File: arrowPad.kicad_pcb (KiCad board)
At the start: 2 copper layers, 59 x 61 mm, 22 parts, among them K1 KEYSW, K2 KEYSW, K3 KEYSW, K4 KEYSW, K5 KEYSW, K6 KEYSW, K7 KEYSW, K8 KEYSW, K9 KEYSW, SW1 SW_DIP_x01, U1 ProMicro, U2 NRF24L01_Breakout

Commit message: added cu ground plane
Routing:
- net /GND1: track 36.0 -> 1.33 mm
- added copper zone on F.Cu, net /GND1
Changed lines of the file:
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@@
     (thickness 1.6)
     (drawings 4)
-    (tracks 233)
+    (tracks 224)
     (zones 0)
     (modules 22)
@@
   (segment (start 80.78 83.63) (end 62.77 83.63) (width 0.25) (layer B.Cu) (net 1))
   (segment (start 61.25 104.52) (end 61.498462 104.52) (width 0.25) (layer F.Cu) (net 2))
-  (segment (start 60.542894 104.52) (end 59.1 103.077106) (width 0.25) (layer B.Cu) (net 2))
   (segment (start 61.25 104.52) (end 60.542894 104.52) (width 0.25) (layer B.Cu) (net 2))
   (via (at 59.1 102.7) (size 0.8) (drill 0.4) (layers F.Cu B.Cu) (net 2))
   (segment (start 59.1 103.077106) (end 59.1 102.7) (width 0.25) (layer B.Cu) (net 2))
-  (segment (start 59.1 95.64) (end 61.8 92.94) (width 0.25) (layer F.Cu) (net 2))
-  (segment (start 59.1 102.7) (end 59.1 95.64) (width 0.25) (layer F.Cu) (net 2))
-  (segment (start 61.8 92.94) (end 62.84 91.9) (width 0.25) (layer F.Cu) (net 2))
-  (segment (start 62.84 91.9) (end 63.3 91.9) (width 0.25) (layer F.Cu) (net 2))
-  (segment (start 63.3 91.9) (end 66.7 88.5) (width 0.25) (layer F.Cu) (net 2))
-  (segment (start 66.7 88.5) (end 72.2 88.5) (width 0.25) (layer F.Cu) (net 2))
-  (segment (start 74.53 86.17) (end 80.78 86.17) (width 0.25) (layer F.Cu) (net 2))
-  (segment (start 72.2 88.5) (end 74.53 86.17) (width 0.25) (layer F.Cu) (net 2))
   (segment (start 43.725 97.375) (end 43.725 96.25) (width 0.25) (layer B.Cu) (net 3))
   (segment (start 48.1 101.75) (end 43.725 97.375) (width 0.25) (layer B.Cu) (net 3))
@@
   (segment (start 61.8 87.55) (end 61.8 90.4) (width 0.25) (layer B.Cu) (net 30))
   (segment (start 59.86 85.61) (end 61.8 87.55) (width 0.25) (layer B.Cu) (net 30))
+  (zone (net 2) (net_name /GND1) (layer F.Cu) (hatch edge 0.508)
+    (connect_pads (clearance 0.254))
+    (min_thickness 0.254)
+    (fill yes (arc_segments 16) (thermal_gap 0.508) (thermal_bridge_width 0.508))
+    (polygon
+      (pts
+        (xy 100.2 81.4) (xy 100.2 142.7) (xy 40.8 142.7) (xy 40.8 81.3)
+      )
+    )
+  )
 )

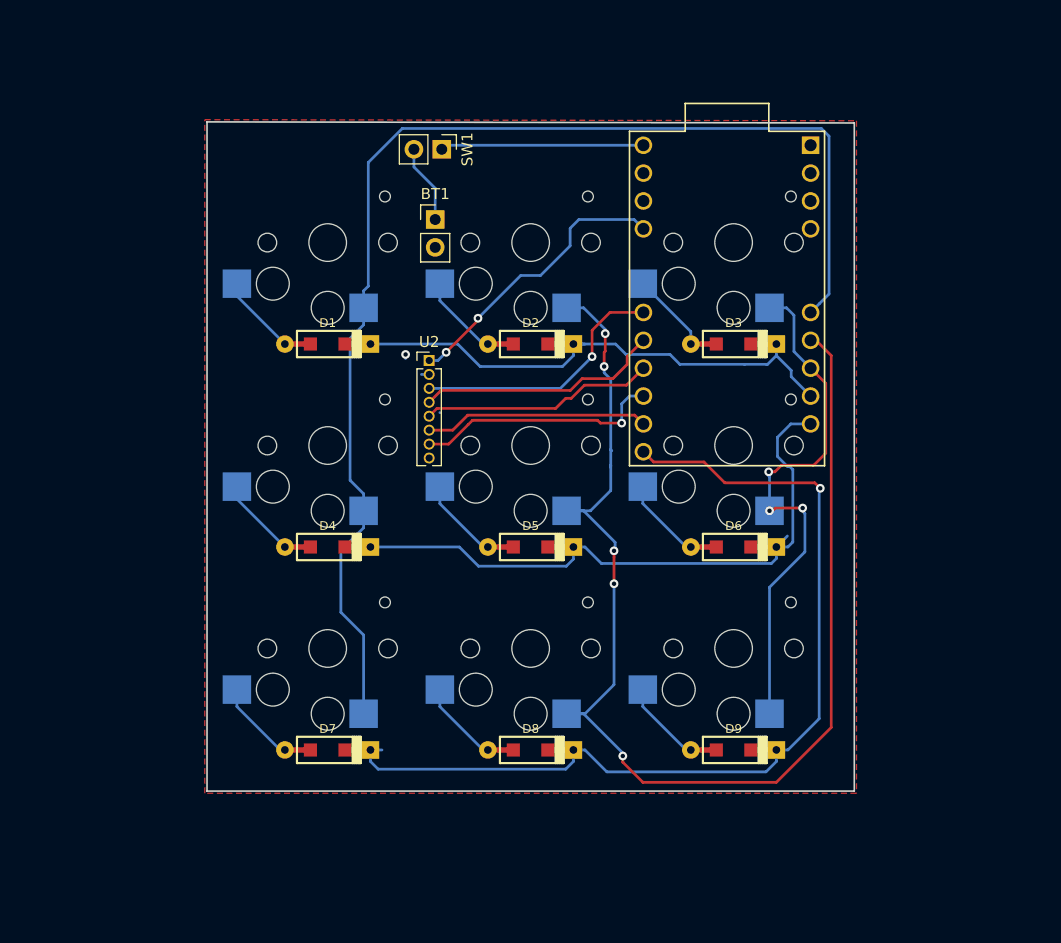
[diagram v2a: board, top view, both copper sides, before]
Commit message: added status led
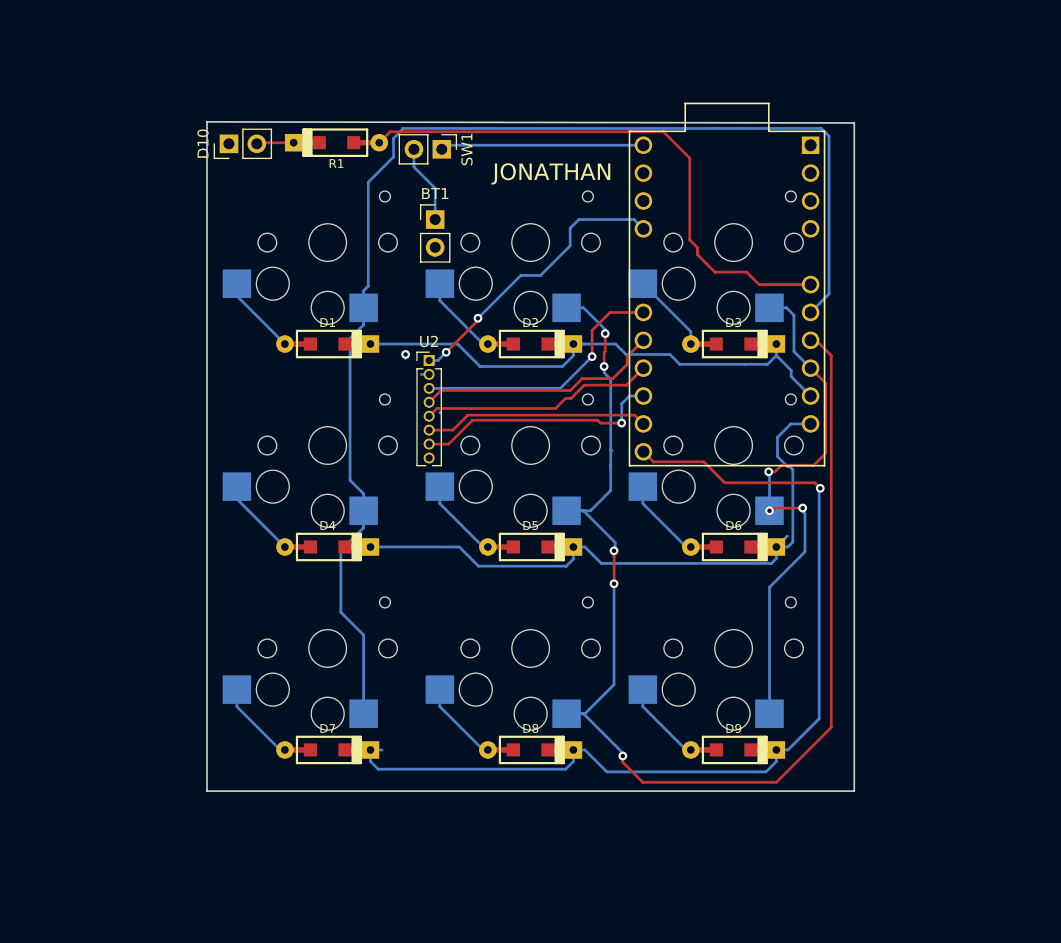
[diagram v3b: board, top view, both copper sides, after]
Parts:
- added D10: LED, Connector_PinHeader_2.54mm:PinHeader_1x02_P2.54mm_Vertical, F.Cu at (43.0, 83.5)
- added R1: R, keyboard_parts:D_SOD123_axial, F.Cu at (52.8, 83.4)
- U1: footprint promicro:proMicrov3 -> Transformer_SMD:proMicrov6
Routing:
- net Net-(R1-Pad2): track 0.00 -> 50.2 mm
- net Net-(D10-Pad2): track 0.00 -> 3.40 mm
- removed copper zone on F.Cu, net /GND1
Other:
- board text added: "JONATHAN"

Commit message: added drill holes
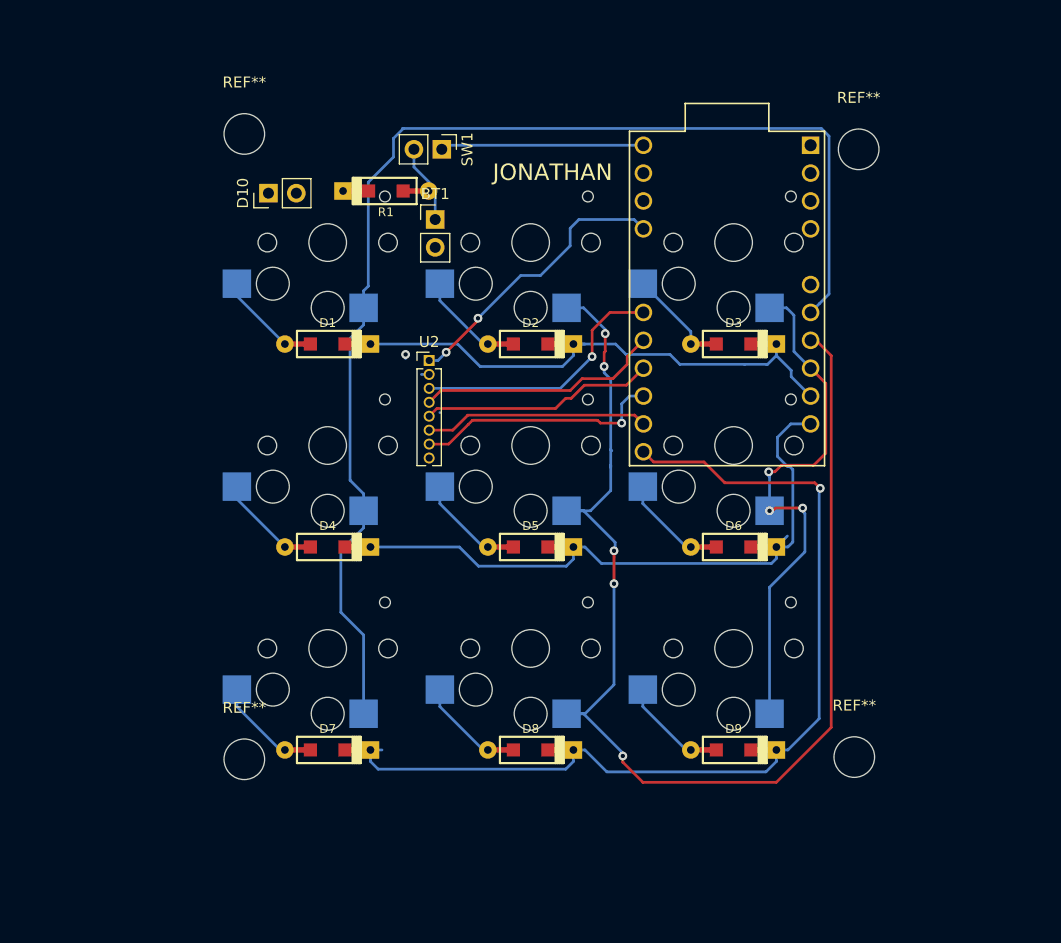
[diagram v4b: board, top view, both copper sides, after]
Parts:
- added REF**: MountingHole_3.7mm, MountingHole:MountingHole_3.7mm, F.Cu at (44.4, 82.6)
- added REF**: MountingHole_3.7mm, MountingHole:MountingHole_3.7mm, F.Cu at (44.4, 139.6)
- added REF**: MountingHole_3.7mm, MountingHole:MountingHole_3.7mm, F.Cu at (100.4, 84.0)
- added REF**: MountingHole_3.7mm, MountingHole:MountingHole_3.7mm, F.Cu at (100.0, 139.4)
- moved R1 6.29 mm to (57.3, 87.8)
- moved D10 5.76 mm to (46.6, 88.0)
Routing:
- net Net-(R1-Pad2): track 50.2 -> 0.00 mm
- net Net-(D10-Pad2): track 3.40 -> 0.00 mm
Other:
- board outline removed
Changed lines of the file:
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@@
   (general
     (thickness 1.6)
-    (drawings 5)
-    (tracks 240)
+    (drawings 6)
+    (tracks 227)
     (zones 0)
-    (modules 24)
+    (modules 28)
     (nets 33)
   )
@@
   )
   (module keyboard_parts:D_SOD123_axial (layer F.Cu)
-    (at 52.8 83.4)
+    (at 57.3 87.8)
     (attr smd)
     (fp_text reference R1 (at 0 1.925) (layer F.SilkS)
@@
   )
   (module Connector_PinHeader_2.54mm:PinHeader_1x02_P2.54mm_Vertical (layer F.Cu)
-    (at 43 83.5 90)
+    (at 46.6 88 90)
     (descr "Through hole straight pin header, 1x02, 2.54mm pitch, single row")
     (tags "Through hole pin header THT 1x02 2.54mm single row")
@@
     )
   )
+  (module MountingHole:MountingHole_3.7mm (layer F.Cu)
+    (at 44.4 82.6)
+    (descr "Mounting Hole 3.7mm, no annular")
+    (tags "mounting hole 3.7mm no annular")
+    (attr virtual)
+    (fp_text reference REF** (at 0 -4.7) (layer F.SilkS)
+      (effects (font (size 1 1) (thickness 0.15)))
+    )
+    (fp_text value MountingHole_3.7mm (at 0 4.7) (layer F.Fab)
+      (effects (font (size 1 1) (thickness 0.15)))
+    )
+    (fp_circle (center 0 0) (end 3.95 0) (layer F.CrtYd) (width 0.05))
+    (fp_circle (center 0 0) (end 3.7 0) (layer Cmts.User) (width 0.15))
+    (fp_text user %R (at 0.3 0) (layer F.Fab)
+      (effects (font (size 1 1) (thickness 0.15)))
+    )
+    (pad 1 np_thru_hole circle (at 0 0) (size 3.7 3.7) (drill 3.7) (layers *.Cu *.Mask))
+  )
+  (module MountingHole:MountingHole_3.7mm (layer F.Cu)
+    (at 44.4 139.6)
+    (descr "Mounting Hole 3.7mm, no annular")
+    (tags "mounting hole 3.7mm no annular")
+    (attr virtual)
+    (fp_text reference REF** (at 0 -4.7) (layer F.SilkS)
+      (effects (font (size 1 1) (thickness 0.15)))
+    )
+    (fp_text value MountingHole_3.7mm (at 0 4.7) (layer F.Fab)
+      (effects (font (size 1 1) (thickness 0.15)))
+    )
+    (fp_circle (center 0 0) (end 3.95 0) (layer F.CrtYd) (width 0.05))
+    (fp_circle (center 0 0) (end 3.7 0) (layer Cmts.User) (width 0.15))
+    (fp_text user %R (at 0.3 0) (layer F.Fab)
+      (effects (font (size 1 1) (thickness 0.15)))
+    )
+    (pad 1 np_thru_hole circle (at 0 0) (size 3.7 3.7) (drill 3.7) (layers *.Cu *.Mask))
+  )
+  (module MountingHole:MountingHole_3.7mm (layer F.Cu)
+    (at 100.4 84)
+    (descr "Mounting Hole 3.7mm, no annular")
+    (tags "mounting hole 3.7mm no annular")
+    (attr virtual)
+    (fp_text reference REF** (at 0 -4.7) (layer F.SilkS)
+      (effects (font (size 1 1) (thickness 0.15)))
+    )
+    (fp_text value MountingHole_3.7mm (at 0 4.7) (layer F.Fab)
+      (effects (font (size 1 1) (thickness 0.15)))
+    )
+    (fp_circle (center 0 0) (end 3.95 0) (layer F.CrtYd) (width 0.05))
+    (fp_circle (center 0 0) (end 3.7 0) (layer Cmts.User) (width 0.15))
+    (fp_text user %R (at 0.3 0) (layer F.Fab)
+      (effects (font (size 1 1) (thickness 0.15)))
+    )
+    (pad 1 np_thru_hole circle (at 0 0) (size 3.7 3.7) (drill 3.7) (layers *.Cu *.Mask))
+  )
+  (module MountingHole:MountingHole_3.7mm (layer F.Cu)
+    (at 100 139.4)
+    (descr "Mounting Hole 3.7mm, no annular")
+    (tags "mounting hole 3.7mm no annular")
+    (attr virtual)
+    (fp_text reference REF** (at 0 -4.7) (layer F.SilkS)
+      (effects (font (size 1 1) (thickness 0.15)))
+    )
+    (fp_text value MountingHole_3.7mm (at 0 4.7) (layer F.Fab)
+      (effects (font (size 1 1) (thickness 0.15)))
+    )
+    (fp_circle (center 0 0) (end 3.95 0) (layer F.CrtYd) (width 0.05))
+    (fp_circle (center 0 0) (end 3.7 0) (layer Cmts.User) (width 0.15))
+    (fp_text user %R (at 0.3 0) (layer F.Fab)
+      (effects (font (size 1 1) (thickness 0.15)))
+    )
+    (pad 1 np_thru_hole circle (at 0 0) (size 3.7 3.7) (drill 3.7) (layers *.Cu *.Mask))
+  )
+  (dimension 7 (width 0.3) (layer F.SilkS)
+    (gr_text "7.000 mm" (at 40.9 66.9) (layer F.SilkS)
+      (effects (font (size 1.5 1.5) (thickness 0.3)))
+    )
+    (feature1 (pts (xy 37.4 85.8) (xy 37.4 68.413579)))
+    (feature2 (pts (xy 44.4 85.8) (xy 44.4 68.413579)))
+    (crossbar (pts (xy 44.4 69) (xy 37.4 69)))
+    (arrow1a (pts (xy 37.4 69) (xy 38.526504 68.413579)))
+    (arrow1b (pts (xy 37.4 69) (xy 38.526504 69.586421)))
+    (arrow2a (pts (xy 44.4 69) (xy 43.273496 68.413579)))
+    (arrow2b (pts (xy 44.4 69) (xy 43.273496 69.586421)))
+  )
+  (dimension 7 (width 0.3) (layer F.SilkS)
+    (gr_text "7.000 mm" (at 100.1 71.7) (layer F.SilkS)
+      (effects (font (size 1.5 1.5) (thickness 0.3)))
+    )
+    (feature1 (pts (xy 103.6 93) (xy 103.6 73.213579)))
+    (feature2 (pts (xy 96.6 93) (xy 96.6 73.213579)))
+    (crossbar (pts (xy 96.6 73.8) (xy 103.6 73.8)))
+    (arrow1a (pts (xy 103.6 73.8) (xy 102.473496 74.386421)))
+    (arrow1b (pts (xy 103.6 73.8) (xy 102.473496 73.213579)))
+    (arrow2a (pts (xy 96.6 73.8) (xy 97.726504 74.386421)))
+    (arrow2b (pts (xy 96.6 73.8) (xy 97.726504 73.213579)))
+  )
+  (dimension 7 (width 0.3) (layer F.SilkS)
+    (gr_text "7.000 mm" (at 108.5 81.5 90) (layer F.SilkS)
+      (effects (font (size 1.5 1.5) (thickness 0.3)))
+    )
+    (feature1 (pts (xy 82.2 78) (xy 106.986421 78)))
+    (feature2 (pts (xy 82.2 85) (xy 106.986421 85)))
+    (crossbar (pts (xy 106.4 85) (xy 106.4 78)))
+    (arrow1a (pts (xy 106.4 78) (xy 106.986421 79.126504)))
+    (arrow1b (pts (xy 106.4 78) (xy 105.813579 79.126504)))
+    (arrow2a (pts (xy 106.4 85) (xy 106.986421 83.873496)))
+    (arrow2b (pts (xy 106.4 85) (xy 105.813579 83.873496)))
+  )
+  (dimension 7 (width 0.3) (layer F.SilkS)
+    (gr_text "7.000 mm" (at 22.1 140.5 270) (layer F.SilkS)
+      (effects (font (size 1.5 1.5) (thickness 0.3)))
+    )
+    (feature1 (pts (xy 65.2 144) (xy 23.613579 144)))
+    (feature2 (pts (xy 65.2 137) (xy 23.613579 137)))
+    (crossbar (pts (xy 24.2 137) (xy 24.2 144)))
+    (arrow1a (pts (xy 24.2 144) (xy 23.613579 142.873496)))
+    (arrow1b (pts (xy 24.2 144) (xy 24.786421 142.873496)))
+    (arrow2a (pts (xy 24.2 137) (xy 23.613579 138.126504)))
+    (arrow2b (pts (xy 24.2 137) (xy 24.786421 138.126504)))
+  )
+  (dimension 7 (width 0.3) (layer F.SilkS)
+    (gr_text "7.000 mm" (at 100.1 157.9) (layer F.SilkS)
+      (effects (font (size 1.5 1.5) (thickness 0.3)))
+    )
+    (feature1 (pts (xy 103.6 122.2) (xy 103.6 156.386421)))
+    (feature2 (pts (xy 96.6 122.2) (xy 96.6 156.386421)))
+    (crossbar (pts (xy 96.6 155.8) (xy 103.6 155.8)))
+    (arrow1a (pts (xy 103.6 155.8) (xy 102.473496 156.386421)))
+    (arrow1b (pts (xy 103.6 155.8) (xy 102.473496 155.213579)))
+    (arrow2a (pts (xy 96.6 155.8) (xy 97.726504 156.386421)))
+    (arrow2b (pts (xy 96.6 155.8) (xy 97.726504 155.213579)))
+  )
   (gr_text JONATHAN (at 72.5 86.1) (layer F.SilkS)
     (effects (font (size 1.5 1.5) (thickness 0.3)))
   )
-  (gr_line (start 41 142.5) (end 41 81.5) (layer Edge.Cuts) (width 0.15))
-  (gr_line (start 100 142.5) (end 41 142.5) (layer Edge.Cuts) (width 0.15))
-  (gr_line (start 100 81.6) (end 100 142.5) (layer Edge.Cuts) (width 0.15))
-  (gr_line (start 41 81.5) (end 100 81.6) (layer Edge.Cuts) (width 0.15))
   (segment (start 62.25 108) (end 62.225001 108) (width 0.25) (layer B.Cu) (net 0))
   (segment (start 62.77 83.63) (end 62.4 84) (width 0.25) (layer B.Cu) (net 1))
@@
   (segment (start 55.7 87) (end 58 84.7) (width 0.25) (layer B.Cu) (net 15))
   (segment (start 58 84.7) (end 58 83) (width 0.25) (layer B.Cu) (net 15))
-  (segment (start 58 83) (end 58.9 82.1) (width 0.25) (layer B.Cu) (net 15))
   (segment (start 58.9 82.1) (end 97 82.1) (width 0.25) (layer B.Cu) (net 15))
   (segment (start 58.8 82.1) (end 58.9 82.1) (width 0.25) (layer B.Cu) (net 15))
+  (segment (start 58 83) (end 58.9 82.1) (width 0.25) (layer B.Cu) (net 15))
   (segment (start 73.775 98.45) (end 73.65 98.45) (width 0.25) (layer B.Cu) (net 16))
   (segment (start 75.325 98.45) (end 77.3 100.425) (width 0.25) (layer B.Cu) (net 16))
@@
   (segment (start 61.8 87.55) (end 61.8 90.4) (width 0.25) (layer B.Cu) (net 30))
   (segment (start 59.86 85.61) (end 61.8 87.55) (width 0.25) (layer B.Cu) (net 30))
-  (segment (start 45.64 83.4) (end 45.54 83.5) (width 0.25) (layer F.Cu) (net 31))
-  (segment (start 48.9 83.4) (end 45.64 83.4) (width 0.25) (layer F.Cu) (net 31))
-  (segment (start 96.02 96.33) (end 91.33 96.33) (width 0.25) (layer F.Cu) (net 32))
-  (segment (start 90.2 95.2) (end 87.3 95.2) (width 0.25) (layer F.Cu) (net 32))
-  (segment (start 91.33 96.33) (end 90.2 95.2) (width 0.25) (layer F.Cu) (net 32))
-  (segment (start 87.3 95.2) (end 85.7 93.6) (width 0.25) (layer F.Cu) (net 32))
-  (segment (start 85.7 92.959666) (end 85 92.259666) (width 0.25) (layer F.Cu) (net 32))
-  (segment (start 85.7 93.6) (end 85.7 92.959666) (width 0.25) (layer F.Cu) (net 32))
-  (segment (start 85 92.259666) (end 85 84.8) (width 0.25) (layer F.Cu) (net 32))
-  (segment (start 85 84.8) (end 82.6 82.4) (width 0.25) (layer F.Cu) (net 32))
-  (segment (start 57.499999 82.600001) (end 56.7 83.4) (width 0.25) (layer F.Cu) (net 32))
-  (segment (start 57.7 82.4) (end 57.499999 82.600001) (width 0.25) (layer F.Cu) (net 32))
-  (segment (start 82.6 82.4) (end 57.7 82.4) (width 0.25) (layer F.Cu) (net 32))
 )
